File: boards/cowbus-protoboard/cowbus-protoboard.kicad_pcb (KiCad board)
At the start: 2 copper layers, 68.7 x 63.7 mm, 42 parts, among them P1 CPU_TO_PERIPH, P2 PERIPH_TO_MCU, P3 SWD, P4 BUZ, P5 USART_DEBUG, P6 CONN_01X02, SW1 SW1, SW2 SW2, SW3 SW3, SW4 SW4, U1 STM32F030C8T6, U2 APE8865N-33-HF-3, U3 nRF24L01+-Module, U4 24C16, U5 LM75AD, Y1 8MHz, Y2 32,768kHz

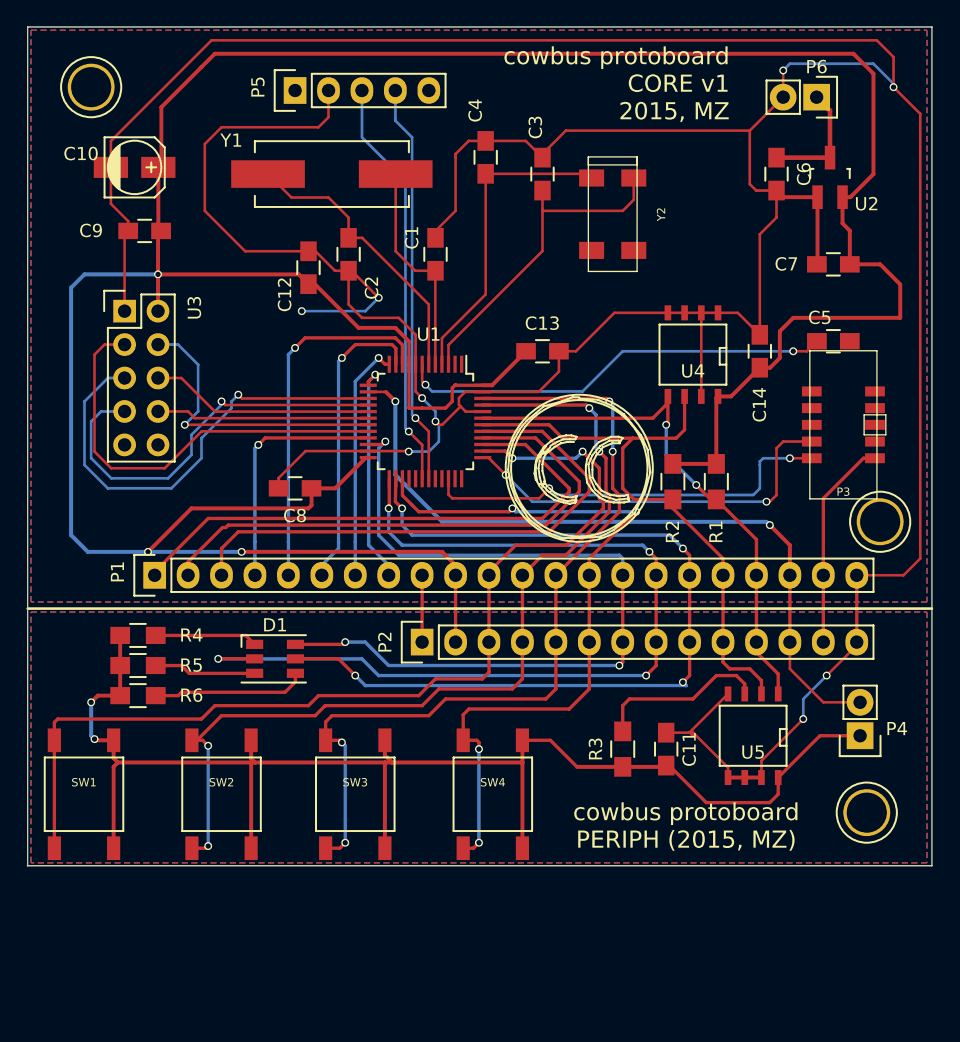
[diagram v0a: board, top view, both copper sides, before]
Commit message: added GPIO18, better 3V3, better GND
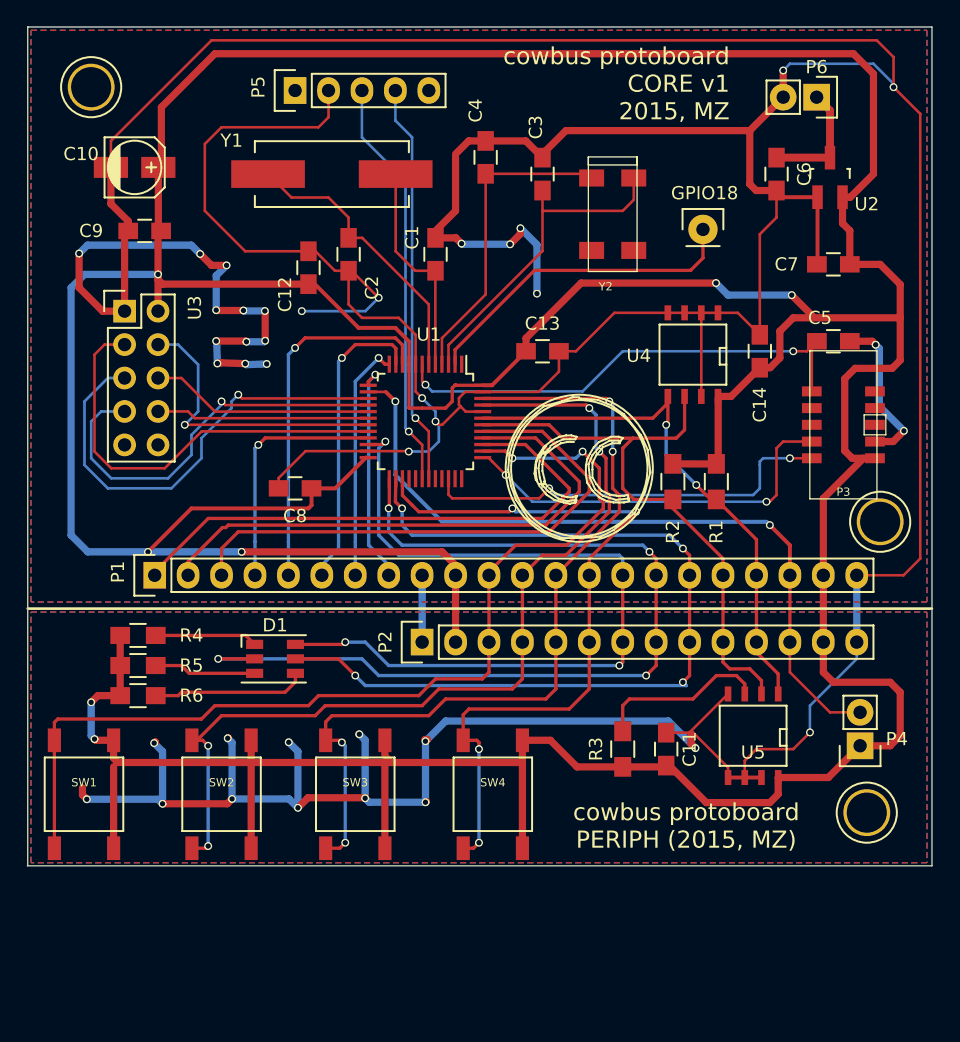
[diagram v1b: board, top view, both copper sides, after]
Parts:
- added GPIO18: CONN_01X01, Pin_Headers:Pin_Header_Straight_1x01, F.Cu at (166.1, 90.6)
- moved P4 0.76 mm to (178.1, 129.8)
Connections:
- U1 pad 2: Net-(U1-Pad2) -> /MCU/GPIO18
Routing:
- net GND: track 340.5 -> 482.2 mm, vias 9 -> 38
- net +3V3: track 363.7 -> 420.3 mm, vias 5 -> 7
- net /MCU/GPIO18: track 0.00 -> 25.0 mm
- net /MCU/NRST: track 33.4 -> 37.4 mm
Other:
- net class 3V3: trace_width 0.254 -> 0.55
- net class Power: trace_width 0.35 -> 0.6

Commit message: wrong LDO pinout corrected + README
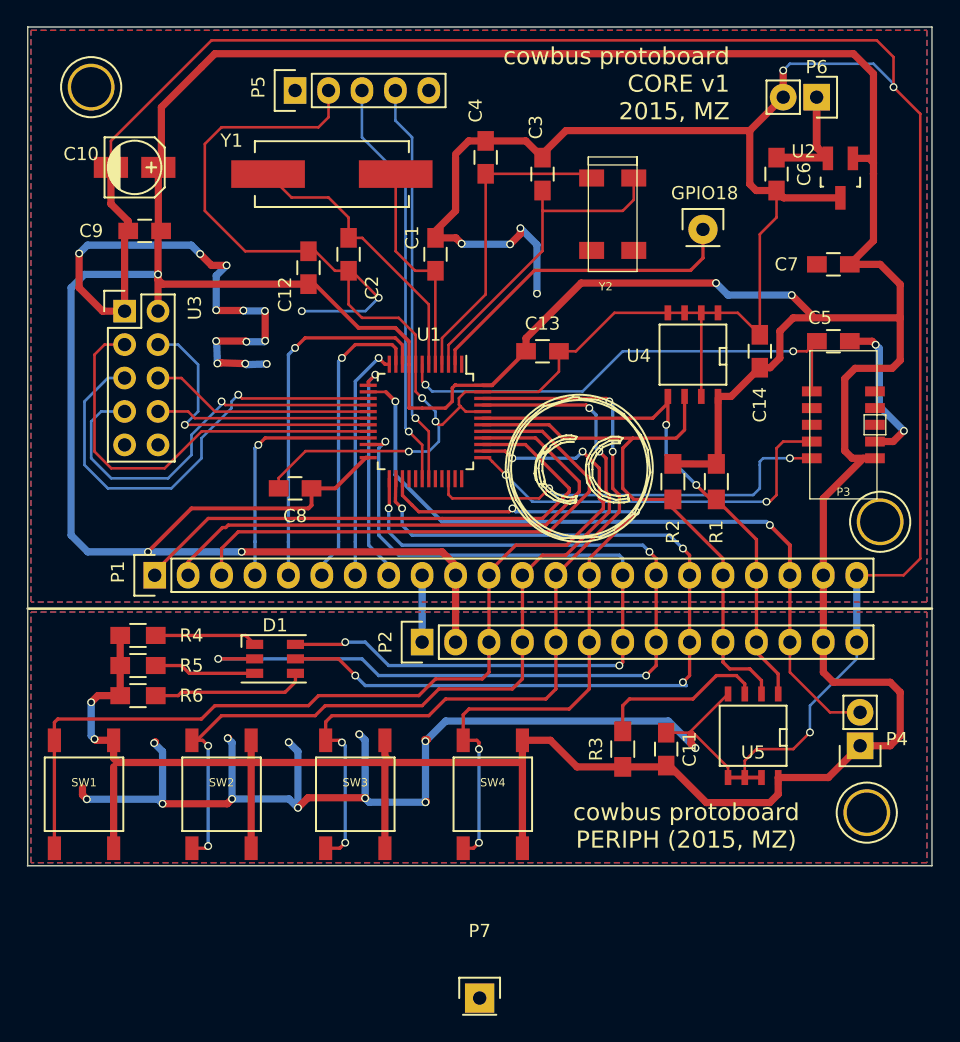
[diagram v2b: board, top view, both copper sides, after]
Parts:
- added P7: CONN_01X01, Pin_Headers:Pin_Header_Straight_1x01, F.Cu at (149.1, 149.0)
- U2: value APE8865N-33-HF-3 -> TS5204
- moved U2 0.79 mm to (176.6, 86.7), turned to 180 degrees
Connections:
- U2 pad 1: GND -> +3V3
- U2 pad 2: +3V3 -> VCC
- U2 pad 3: VCC -> GND
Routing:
- net GND: track 482.2 -> 479.6 mm
- net +3V3: track 420.3 -> 421.3 mm
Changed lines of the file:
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@@
 (kicad_pcb (version 4) (host pcbnew 0.201507310902+6023~28~ubuntu14.04.1-product)
   (general
-    (links 143)
-    (no_connects 0)
+    (links 144)
+    (no_connects 1)
     (area 114.734999 75.133999 183.562601 138.962601)
     (thickness 1.6)
     (drawings 7)
-    (tracks 803)
+    (tracks 804)
     (zones 0)
-    (modules 43)
+    (modules 44)
     (nets 55)
   )
@@
   )
   (module Housings_SOT-23_SOT-143_TSOT-6:SOT-23_Handsoldering (layer F.Cu)
-    (at 175.768 86.614)
+    (at 176.5554 86.6648 180)
     (descr "SOT-23, Handsoldering")
     (tags SOT-23)
     (attr smd)
-    (fp_text reference U2 (at 2.794 2.032) (layer F.SilkS)
-      (effects (font (size 1 1) (thickness 0.15)))
-    )
-    (fp_text value APE8865N-33-HF-3 (at 0 3.81) (layer F.Fab)
+    (fp_text reference U2 (at 2.794 2.032 180) (layer F.SilkS)
+      (effects (font (size 1 1) (thickness 0.15)))
+    )
+    (fp_text value TS5204 (at 0 3.81 180) (layer F.Fab)
       (effects (font (size 1 1) (thickness 0.15)))
     )
@@
     (fp_line (start 1.29916 -0.65024) (end 1.49982 -0.65024) (layer F.SilkS) (width 0.15))
     (fp_line (start 1.49982 -0.65024) (end 1.49982 0.0508) (layer F.SilkS) (width 0.15))
-    (pad 1 smd rect (at -0.95 1.50114) (size 0.8001 1.80086) (layers F.Cu F.Paste F.Mask)
-      (net 2 GND))
-    (pad 2 smd rect (at 0.95 1.50114) (size 0.8001 1.80086) (layers F.Cu F.Paste F.Mask)
-      (net 8 +3V3))
-    (pad 3 smd rect (at 0 -1.50114) (size 0.8001 1.80086) (layers F.Cu F.Paste F.Mask)
+    (pad 1 smd rect (at -0.95 1.50114 180) (size 0.8001 1.80086) (layers F.Cu F.Paste F.Mask)
+      (net 8 +3V3))
+    (pad 2 smd rect (at 0.95 1.50114 180) (size 0.8001 1.80086) (layers F.Cu F.Paste F.Mask)
       (net 7 VCC))
+    (pad 3 smd rect (at 0 -1.50114 180) (size 0.8001 1.80086) (layers F.Cu F.Paste F.Mask)
+      (net 2 GND))
     (model Housings_SOT-23_SOT-143_TSOT-6.3dshapes/SOT-23_Handsoldering.wrl
       (at (xyz 0 0 0))
@@
     )
   )
+  (module Pin_Headers:Pin_Header_Straight_1x01 (layer F.Cu)
+    (at 149.1488 148.962601)
+    (descr "Through hole pin header")
+    (tags "pin header")
+    (fp_text reference P7 (at 0 -5.1) (layer F.SilkS)
+      (effects (font (size 1 1) (thickness 0.15)))
+    )
+    (fp_text value CONN_01X01 (at 0 -3.1) (layer F.Fab)
+      (effects (font (size 1 1) (thickness 0.15)))
+    )
+    (fp_line (start 1.55 -1.55) (end 1.55 0) (layer F.SilkS) (width 0.15))
+    (fp_line (start -1.75 -1.75) (end -1.75 1.75) (layer F.CrtYd) (width 0.05))
+    (fp_line (start 1.75 -1.75) (end 1.75 1.75) (layer F.CrtYd) (width 0.05))
+    (fp_line (start -1.75 -1.75) (end 1.75 -1.75) (layer F.CrtYd) (width 0.05))
+    (fp_line (start -1.75 1.75) (end 1.75 1.75) (layer F.CrtYd) (width 0.05))
+    (fp_line (start -1.55 0) (end -1.55 -1.55) (layer F.SilkS) (width 0.15))
+    (fp_line (start -1.55 -1.55) (end 1.55 -1.55) (layer F.SilkS) (width 0.15))
+    (fp_line (start -1.27 1.27) (end 1.27 1.27) (layer F.SilkS) (width 0.15))
+    (pad 1 thru_hole rect (at 0 0) (size 2.2352 2.2352) (drill 1.016) (layers *.Cu *.Mask F.SilkS)
+      (net 54 /MCU/GPIO18))
+    (model Pin_Headers.3dshapes/Pin_Header_Straight_1x01.wrl
+      (at (xyz 0 0 0))
+      (scale (xyz 1 1 1))
+      (rotate (xyz 0 0 90))
+    )
+  )
   (gr_text "cowbus protoboard\nCORE v1\n2015, MZ" (at 168.148 79.502) (layer F.SilkS)
     (effects (font (size 1.3 1.3) (thickness 0.25)) (justify right))
@@
   (segment (start 145.784 100.806) (end 145.784 93.718) (width 0.2) (layer F.Cu) (net 1))
   (segment (start 145.784 93.718) (end 145.796 93.706) (width 0.2) (layer F.Cu) (net 1))
+  (segment (start 176.5554 88.16594) (end 172.25994 88.16594) (width 0.55) (layer F.Cu) (net 2) (status C00000))
+  (segment (start 172.25994 88.16594) (end 171.704 87.61) (width 0.55) (layer F.Cu) (net 2) (status C00000))
   (segment (start 122.174 96.774) (end 120.4976 96.774) (width 0.55) (layer F.Cu) (net 2))
   (segment (start 132.969 100.7872) (end 132.9944 100.7872) (width 0.55) (layer F.Cu) (net 2))
@@
   (segment (start 133.878 109.454) (end 133.878 110.236) (width 0.2) (layer F.Cu) (net 2))
   (segment (start 135.926 107.406) (end 133.878 109.454) (width 0.2) (layer F.Cu) (net 2))
-  (segment (start 174.818 88.11514) (end 172.20914 88.11514) (width 0.3) (layer F.Cu) (net 2))
   (segment (start 172.20914 88.11514) (end 171.704 87.61) (width 0.3) (layer F.Cu) (net 2))
-  (segment (start 174.818 88.11514) (end 174.818 93.172) (width 0.3) (layer F.Cu) (net 2))
   (segment (start 174.818 93.172) (end 174.772 93.218) (width 0.3) (layer F.Cu) (net 2))
   (segment (start 169.291 132.207) (end 168.021 132.207) (width 0.3) (layer F.Cu) (net 2))
@@
   (via (at 145.034 102.362) (size 0.6) (drill 0.4) (layers F.Cu B.Cu) (net 6))
   (segment (start 144.784 102.112) (end 145.034 102.362) (width 0.2) (layer F.Cu) (net 6))
-  (segment (start 171.704 85.11) (end 175.76514 85.11) (width 0.6) (layer F.Cu) (net 7))
-  (segment (start 175.76514 85.11) (end 175.768 85.11286) (width 0.35) (layer F.Cu) (net 7))
-  (segment (start 175.768 85.11286) (end 175.768 81.534) (width 0.6) (layer F.Cu) (net 7))
-  (segment (start 175.768 81.534) (end 174.752 80.518) (width 0.6) (layer F.Cu) (net 7))
+  (segment (start 174.752 80.518) (end 174.752 84.31026) (width 0.6) (layer F.Cu) (net 7) (status 400000))
+  (segment (start 174.752 84.31026) (end 175.6054 85.16366) (width 0.6) (layer F.Cu) (net 7) (status 800000))
+  (segment (start 171.704 85.11) (end 175.55174 85.11) (width 0.6) (layer F.Cu) (net 7) (status C00000))
+  (segment (start 175.55174 85.11) (end 175.6054 85.16366) (width 0.6) (layer F.Cu) (net 7) (status C00000))
+  (segment (start 177.5054 85.16366) (end 178.73726 85.16366) (width 0.55) (layer F.Cu) (net 8) (status 400000))
+  (segment (start 178.73726 85.16366) (end 179.07 85.4964) (width 0.55) (layer F.Cu) (net 8))
+  (segment (start 179.07 86.3092) (end 179.07 91.42) (width 0.55) (layer F.Cu) (net 8))
+  (segment (start 179.07 91.42) (end 177.272 93.218) (width 0.55) (layer F.Cu) (net 8) (status 800000))
+  (segment (start 179.07 86.36) (end 179.07 86.3092) (width 0.55) (layer F.Cu) (net 8))
+  (segment (start 179.07 86.3092) (end 179.07 85.4964) (width 0.55) (layer F.Cu) (net 8))
+  (segment (start 179.07 85.4964) (end 179.07 78.74) (width 0.55) (layer F.Cu) (net 8))
+  (segment (start 179.07 78.74) (end 177.546 77.216) (width 0.55) (layer F.Cu) (net 8))
+  (segment (start 177.546 77.216) (end 129.032 77.216) (width 0.55) (layer F.Cu) (net 8))
   (segment (start 175.26 121.92) (end 175.26 116.84) (width 0.55) (layer F.Cu) (net 8))
   (segment (start 147.32 116.84) (end 147.32 121.92) (width 0.55) (layer F.Cu) (net 8))
@@
   (segment (start 174.3837 97.282) (end 181.102 97.282) (width 0.55) (layer F.Cu) (net 8))
   (segment (start 179.578 93.218) (end 181.102 94.742) (width 0.55) (layer F.Cu) (net 8))
+  (segment (start 181.102 94.742) (end 181.102 97.282) (width 0.55) (layer F.Cu) (net 8))
   (segment (start 179.578 93.218) (end 177.272 93.218) (width 0.55) (layer F.Cu) (net 8))
-  (segment (start 181.102 94.742) (end 181.102 97.282) (width 0.55) (layer F.Cu) (net 8))
   (segment (start 136.144 94.234) (end 136.144 94.234) (width 0.3) (layer F.Cu) (net 8))
   (segment (start 168.255 103.251) (end 170.434 101.072) (width 0.55) (layer F.Cu) (net 8))
@@
   (segment (start 124.73686 90.46686) (end 124.948 90.678) (width 0.3) (layer F.Cu) (net 8))
   (segment (start 128.016 78.232) (end 124.968 81.28) (width 0.55) (layer F.Cu) (net 8))
-  (segment (start 177.31486 88.11514) (end 179.07 86.36) (width 0.55) (layer F.Cu) (net 8))
-  (segment (start 179.07 86.36) (end 179.07 78.74) (width 0.55) (layer F.Cu) (net 8))
-  (segment (start 179.07 78.74) (end 177.546 77.216) (width 0.55) (layer F.Cu) (net 8))
-  (segment (start 177.546 77.216) (end 129.032 77.216) (width 0.55) (layer F.Cu) (net 8))
   (segment (start 129.032 77.216) (end 128.016 78.232) (width 0.55) (layer F.Cu) (net 8))
-  (segment (start 176.718 88.11514) (end 177.31486 88.11514) (width 0.55) (layer F.Cu) (net 8))
   (segment (start 124.968 81.28) (end 124.968 85.62086) (width 0.55) (layer F.Cu) (net 8))
   (segment (start 124.968 85.62086) (end 124.73686 85.852) (width 0.3) (layer F.Cu) (net 8))
@@
   (segment (start 140.506 107.906) (end 138.176 110.236) (width 0.3) (layer F.Cu) (net 8))
   (segment (start 138.176 110.236) (end 136.378 110.236) (width 0.3) (layer F.Cu) (net 8))
-  (segment (start 176.718 88.11514) (end 176.718 90.104) (width 0.55) (layer F.Cu) (net 8))
-  (segment (start 176.718 90.104) (end 177.272 90.658) (width 0.55) (layer F.Cu) (net 8))
-  (segment (start 177.272 90.658) (end 177.272 93.218) (width 0.55) (layer F.Cu) (net 8))
   (segment (start 167.3987 103.251) (end 168.255 103.251) (width 0.55) (layer F.Cu) (net 8))
   (segment (start 167.2717 108.3818) (end 167.2717 103.378) (width 0.55) (layer F.Cu) (net 8))

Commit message: added schematics rev, annotation fixed, OSHW logo
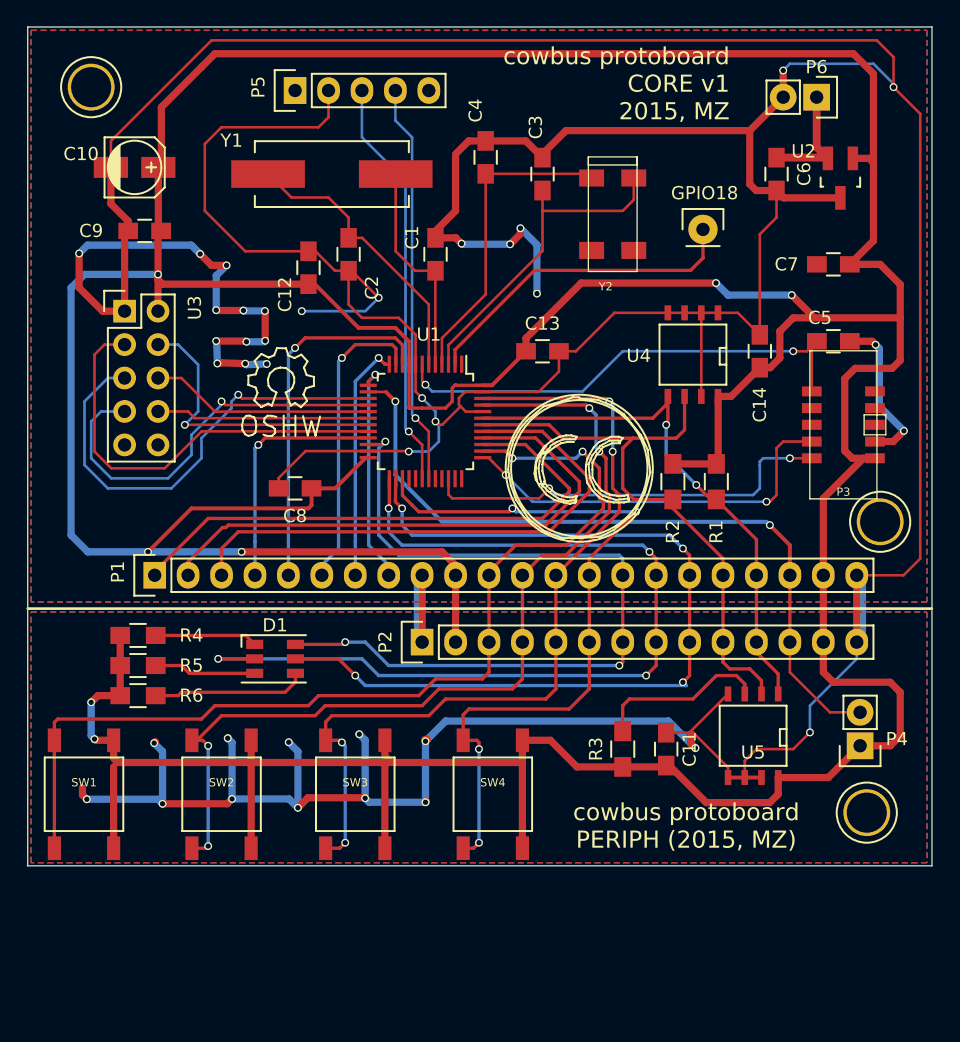
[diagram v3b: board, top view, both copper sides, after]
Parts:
- removed P7: CONN_01X01, Pin_Headers:Pin_Header_Straight_1x01
- added ?: Symbol_OSHW-Logo_SilkScreen, Symbols:Symbol_OSHW-Logo_SilkScreen, F.Cu at (134.1, 102.1)
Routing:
- net GND: track 479.6 -> 490.4 mm
